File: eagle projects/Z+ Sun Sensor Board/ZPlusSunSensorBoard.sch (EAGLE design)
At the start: 51 parts, among them Q2 BSS138, Q4 BSS138, Q6 BSS138, Q8 BSS138, U1 ADS7841E_2K5, U2 REF194GSZ-REEL7, U3 TLV9054IDR, U4 LM20BIM7X_NOPB

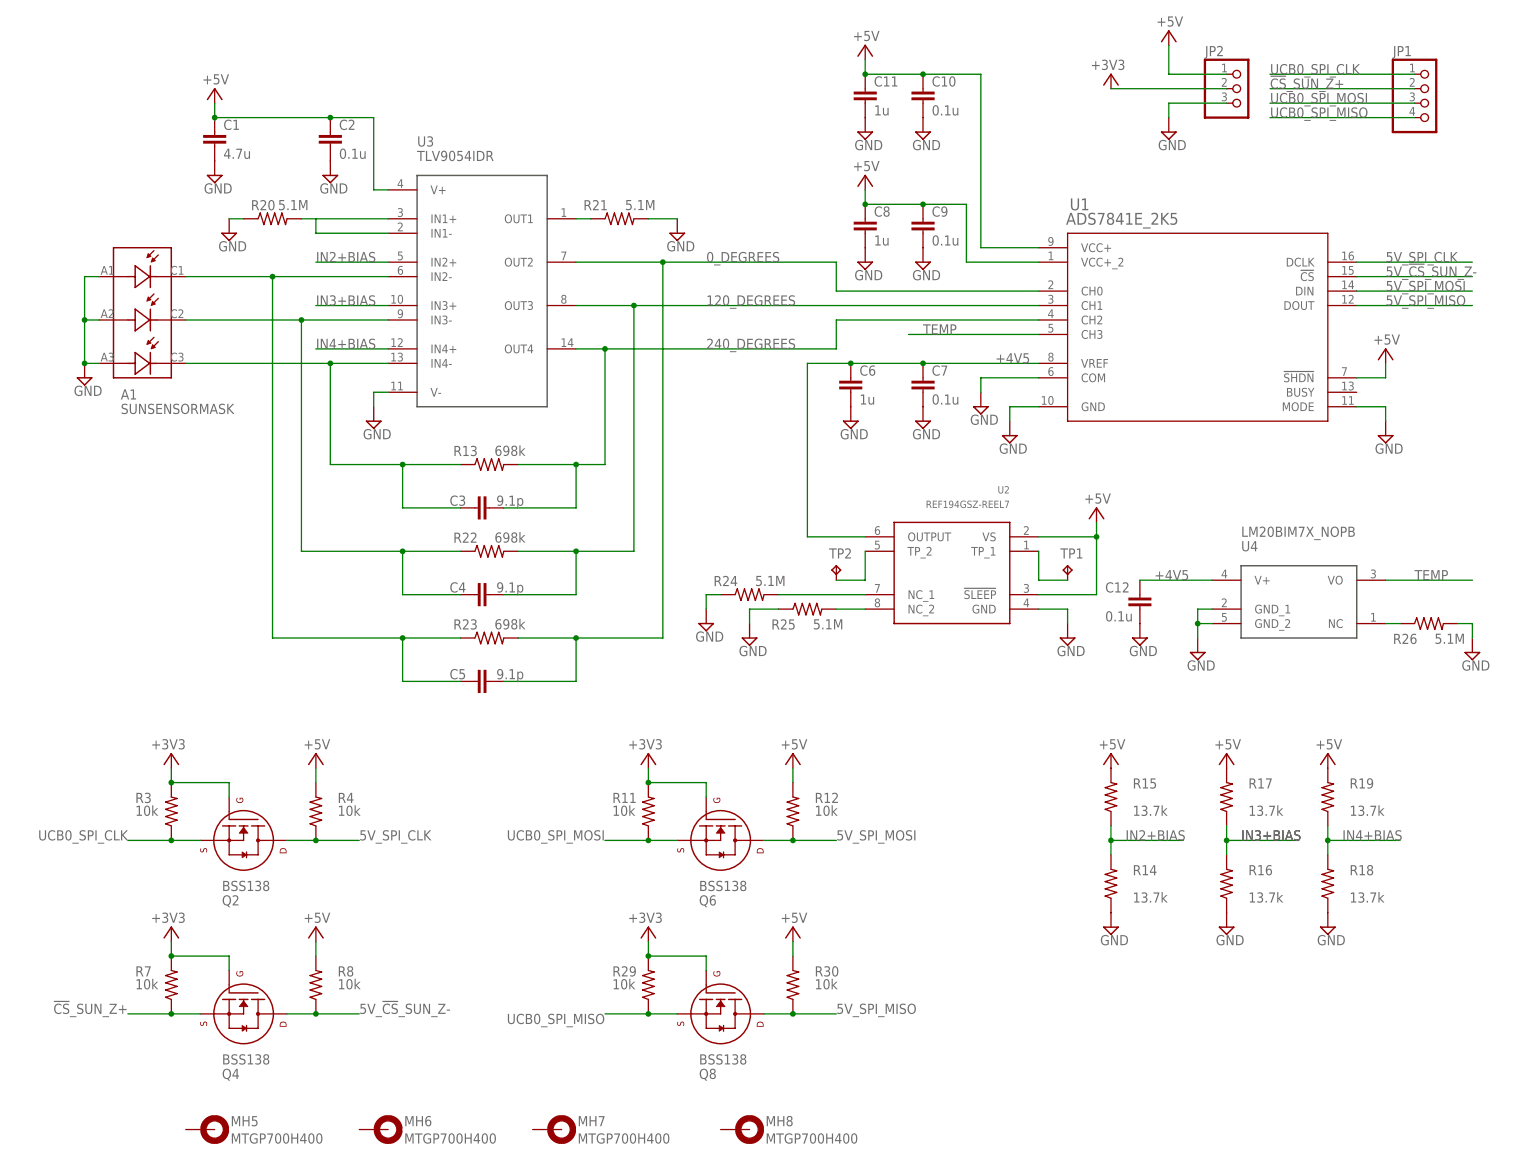
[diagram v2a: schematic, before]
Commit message: New sunsensor layout and updated sun sensor mask mount
now all on 3v3 supply
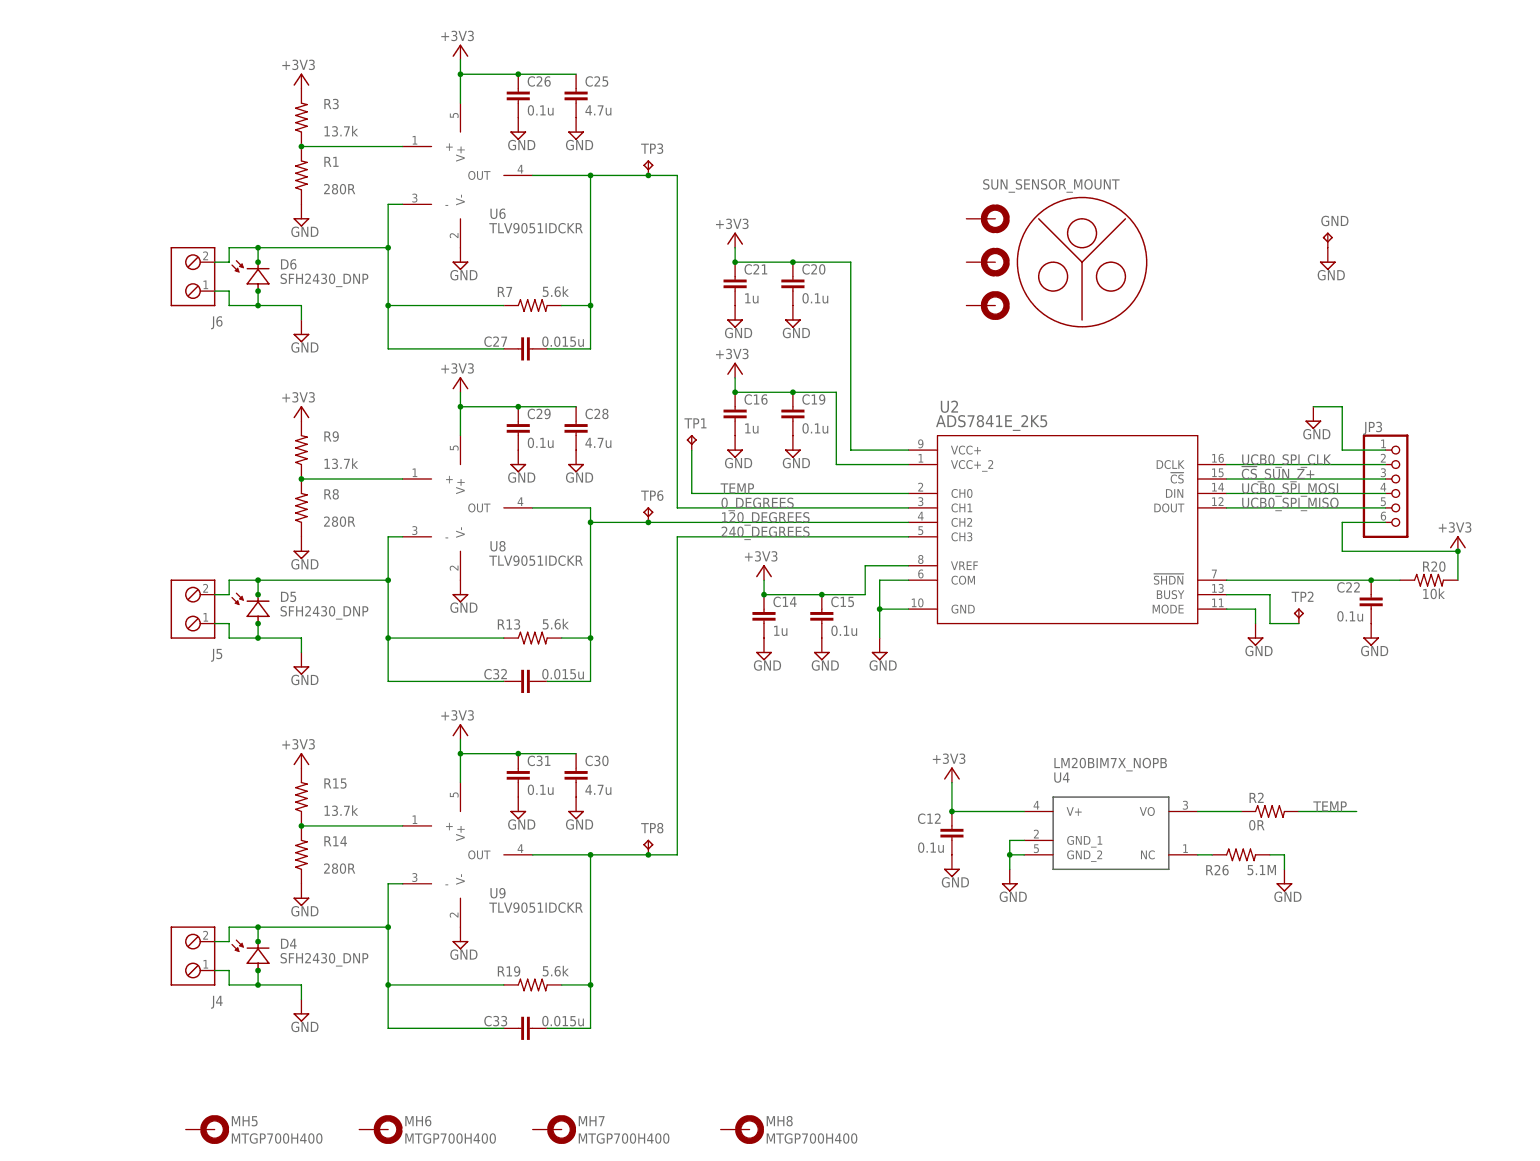
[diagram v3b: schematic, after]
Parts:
- removed C1: 4.7u, rcl:C-EUC0603
- removed C10, C2, C7, C9: 0.1u, rcl:C-EUC0603
- removed C11, C6, C8: 1u, rcl:C-EUC0603
- removed C3, C4, C5: 9.1p, rcl:C-EUC0603
- removed JP1: (no value), pinhead:PINHD-1X4
- removed JP2: (no value), pinhead:PINHD-1X3
- removed Q2, Q4, Q6, Q8: BSS138, my_library:BSS138
- removed R11, R12, R29, R30, R4: 10k, rcl:R-US_R0603
- removed R16, R17, R18: 13.7k, rcl:R-US_R0603
- removed R21, R24, R25: 5.1M, rcl:R-US_R0603
- removed R22, R23: 698k, rcl:R-US_R0603
- removed U1: ADS7841E_2K5, my_library:ADS7841E_2K5
- removed U3: TLV9054IDR, my_library:TLV9054IDR
- added C14, C16, C21: 1u, resistor:C-EUC0402
- added C15, C19, C20, C22, C26, C29, C31: 0.1u, resistor:C-EUC0402
- added C25, C28, C30: 4.7u, rcl:C-EUC0805
- added C27, C32, C33: 0.015u, resistor:C-EUC0402
- added GND, TP3, TP6, TP8: TESTPOINT, my_library:TESTPOINT
- added J4, J5, J6: (no value), my_library:TRM_BLK_1X2
- added JP3: (no value), pinhead:PINHD-1X6
- added R1: 280R, resistor:R-US_R0402
- added R2: 0R, rcl:R-US_R0805
- added R9: 13.7k, resistor:R-US_R0402
- added U6, U8, U9: TLV9051IDCKR, my_library:TLV9051IDCKR
- A1: value SUNSENSORMASK -> SUN_SENSOR_MOUNT; device my_library:SUNSENSORMASK -> my_library:SUN_SENSOR_MOUNT
- R13: value 698k -> 5.6k; device rcl:R-US_R0603 -> resistor:R-US_R0402
- R14: value 13.7k -> 280R; device rcl:R-US_R0603 -> resistor:R-US_R0402
- R15: device rcl:R-US_R0603 -> resistor:R-US_R0402
- R19: value 13.7k -> 5.6k; device rcl:R-US_R0603 -> resistor:R-US_R0402
- R20: value 5.1M -> 10k; device rcl:R-US_R0603 -> resistor:R-US_R0402
- R3: value 10k -> 13.7k; device rcl:R-US_R0603 -> resistor:R-US_R0402
- R7: value 10k -> 5.6k; device rcl:R-US_R0603 -> resistor:R-US_R0402
- R8: value 10k -> 280R; device rcl:R-US_R0603 -> resistor:R-US_R0402
- TP1, TP2: value TPB1,27 -> TESTPOINT; device testpad:TPB1,27 -> my_library:TESTPOINT
- U2: value REF194GSZ-REEL7 -> ADS7841E_2K5; device my_library:REF194GSZ-REEL7 -> my_library:ADS7841E_2K5
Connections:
- removed net +4V5: C12.1, C6.1, C7.1, U1.VREF, U2.OUTPUT, U4.V+
- removed net +5V: C1.1, C10.1, C11.1, C2.1, C8.1, C9.1, JP2.1, R12.2, R15.2, R17.2, R19.2, R30.2, R4.2, R8.2, U1.!SHDN, U1.VCC+, U1.VCC+_2, U2.!SLEEP, U2.VS, U3.V+
- removed net 5V_!CS!_SUN_Z-: Q4.D, R8.1, U1.!CS
- removed net 5V_SPI_CLK: Q2.D, R4.1, U1.DCLK
- removed net 5V_SPI_MISO: Q8.D, R30.1, U1.DOUT
- removed net 5V_SPI_MOSI: Q6.D, R12.1, U1.DIN
- removed net IN2+BIAS: R14.2, R15.1, U3.IN2+
- removed net IN3+BIAS: R16.2, R17.1, U3.IN3+
- removed net IN4+BIAS: R18.2, R19.1, U3.IN4+
- removed net N$10: TP2.TP, U2.TP_2
- removed net N$11: TP1.TP, U2.TP_1
- removed net N$14: A1.C2, C4.1, R22.1, U3.IN3-
- removed net N$5: R20.2, U3.IN1+, U3.IN1-
- new net N$1: R2.1, U4.VO
- new net N$2: TP2.TP, U2.BUSY
- new net N$3: C27.1, J6.2, R7.1, U6.-
- new net N$8: C32.1, J5.2, R13.1, U8.-
- net !CS!_SUN_Z+: now also JP3.3, U2.!CS; no longer JP1.2, Q4.S, R7.1
- net +3V3: now also C12.1, C14.1, C15.1, C16.1, C19.1, C20.1, C21.1, C25.1, C26.1, C28.1, C29.1, C30.1, C31.1, JP3.6, R15.2, R20.2, R9.2, U2.VCC+, U2.VCC+_2, U2.VREF, U4.V+, U6.V+, U8.V+, U9.V+; no longer JP2.2, Q2.G, Q4.G, Q6.G, Q8.G, R11.2, R29.2, R7.2
- net 0_DEGREES: now also C27.2, R7.2, TP3.TP, U2.CH1, U6.OUT; no longer C5.2, R23.2, U1.CH0, U3.OUT2
- net 120_DEGREES: now also C32.2, R13.2, TP6.TP, U2.CH2, U8.OUT; no longer C4.2, R22.2, U1.CH1, U3.OUT3
- net 240_DEGREES: now also C33.2, R19.2, TP8.TP, U2.CH3, U9.OUT; no longer C3.2, R13.2, U1.CH2, U3.OUT4
- net GND: now also C14.2, C15.2, C16.2, C19.2, C20.2, C21.2, C22.2, C25.2, C26.2, C28.2, C29.2, C30.2, C31.2, GND.TP, J4.1, J5.1, J6.1, JP3.1, R1.1, R8.1, U2.COM, U2.MODE, U6.V-, U8.V-, U9.V-; no longer A1.A1, A1.A2, A1.A3, C1.2, C10.2, C11.2, C2.2, C6.2, C7.2, C8.2, C9.2, JP2.3, R16.1, R18.1, R20.1, R21.2, R24.1, R25.1, U1.COM, U1.GND, U1.MODE, U3.V-
- net N$12: now also C33.1, J4.2, R19.1, U9.-; no longer R24.2, U2.NC_1
- net N$13: now also R14.2, R15.1, U9.+; no longer R25.2, U2.NC_2
- net N$15: now also C22.1, R20.1, U2.!SHDN; no longer A1.C3, C3.1, R13.1, U3.IN4-
- net N$6: now also R1.2, R3.1, U6.+; no longer R21.1, U3.OUT1
- net N$9: now also R8.2, R9.1, U8.+; no longer A1.C1, C5.1, R23.1, U3.IN2-
- net TEMP: now also R2.2, TP1.TP, U2.CH0; no longer U1.CH3, U4.VO
- net UCB0_SPI_CLK: now also JP3.2, U2.DCLK; no longer JP1.1, Q2.S, R3.1
- net UCB0_SPI_MISO: now also JP3.5, U2.DOUT; no longer JP1.4, Q8.S, R29.1
- net UCB0_SPI_MOSI: now also JP3.4, U2.DIN; no longer JP1.3, Q6.S, R11.1
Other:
- moved on the sheet: C12, R13, R14, R15, R19, R20, R26, R3, R7, R8, TP1, TP2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
